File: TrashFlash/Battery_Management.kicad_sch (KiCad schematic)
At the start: 20 parts, among them IC701 BQ27426YZFR, IC702 BQ24230RGTR, IC703 BQ29732DSER, J701 USB4800-03-A, Q701 PMDPB30XNAX

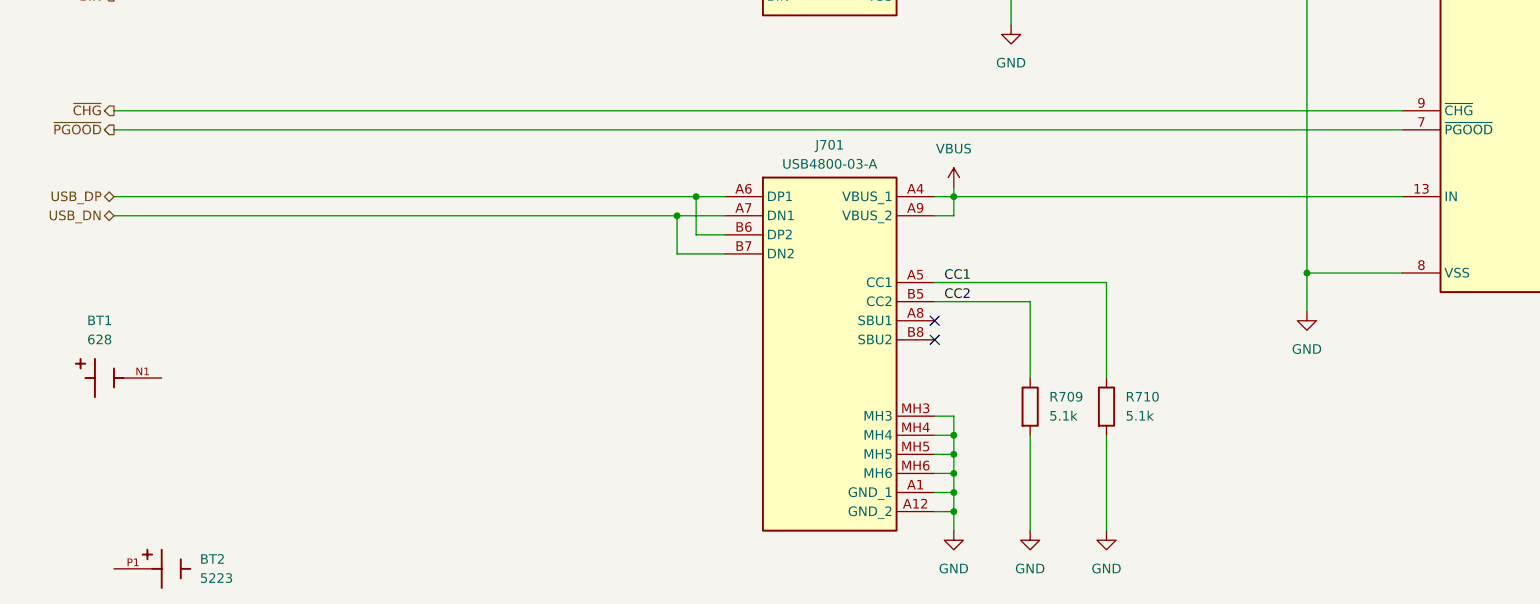
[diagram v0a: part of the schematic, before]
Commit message: Moved USB and added JTAG connector
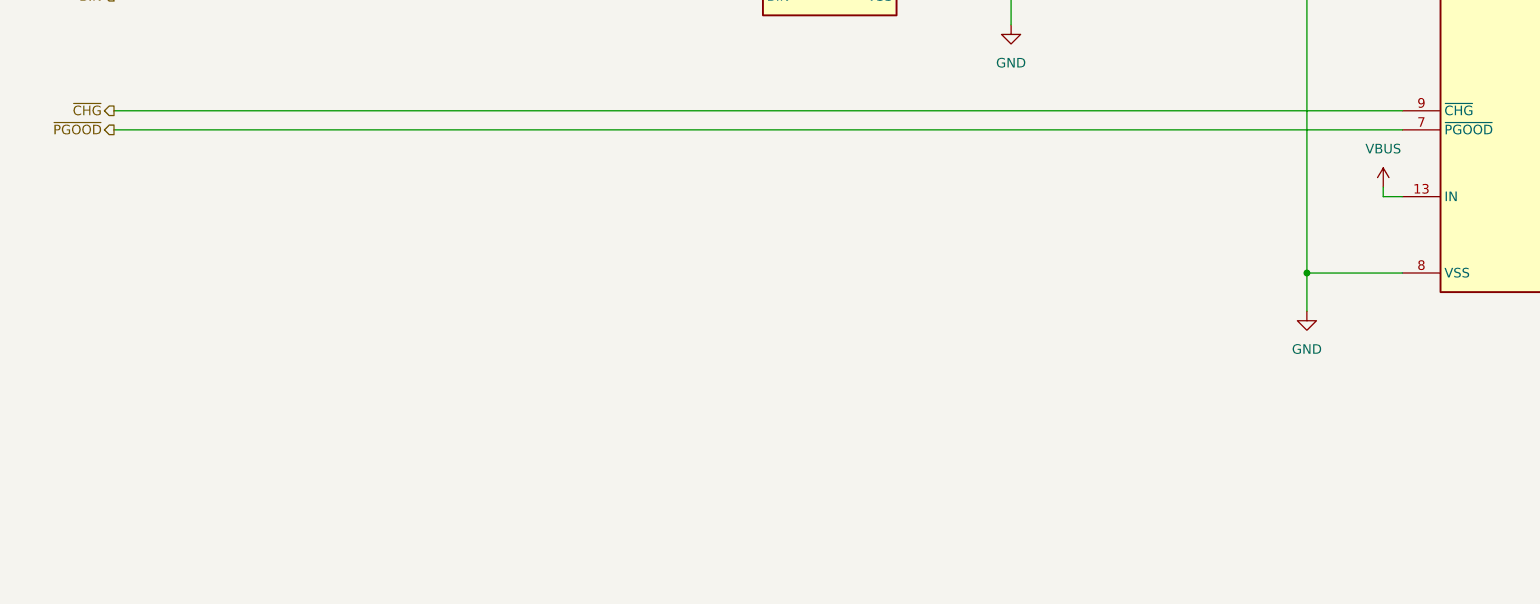
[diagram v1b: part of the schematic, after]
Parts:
- removed BT1: 628, TrashFlash:BAT_628, symbol TrashFlash:628
- removed BT2: 5223, TrashFlash:BAT_5223, symbol TrashFlash:5223
- removed J701: USB4800-03-A, USB480003A, symbol TrashFlash:USB4800-03-A
- removed R709, R710: 5.1k, Resistor_SMD:R_0402_1005Metric, symbol Device:R
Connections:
- no-connect marks 2 -> 0

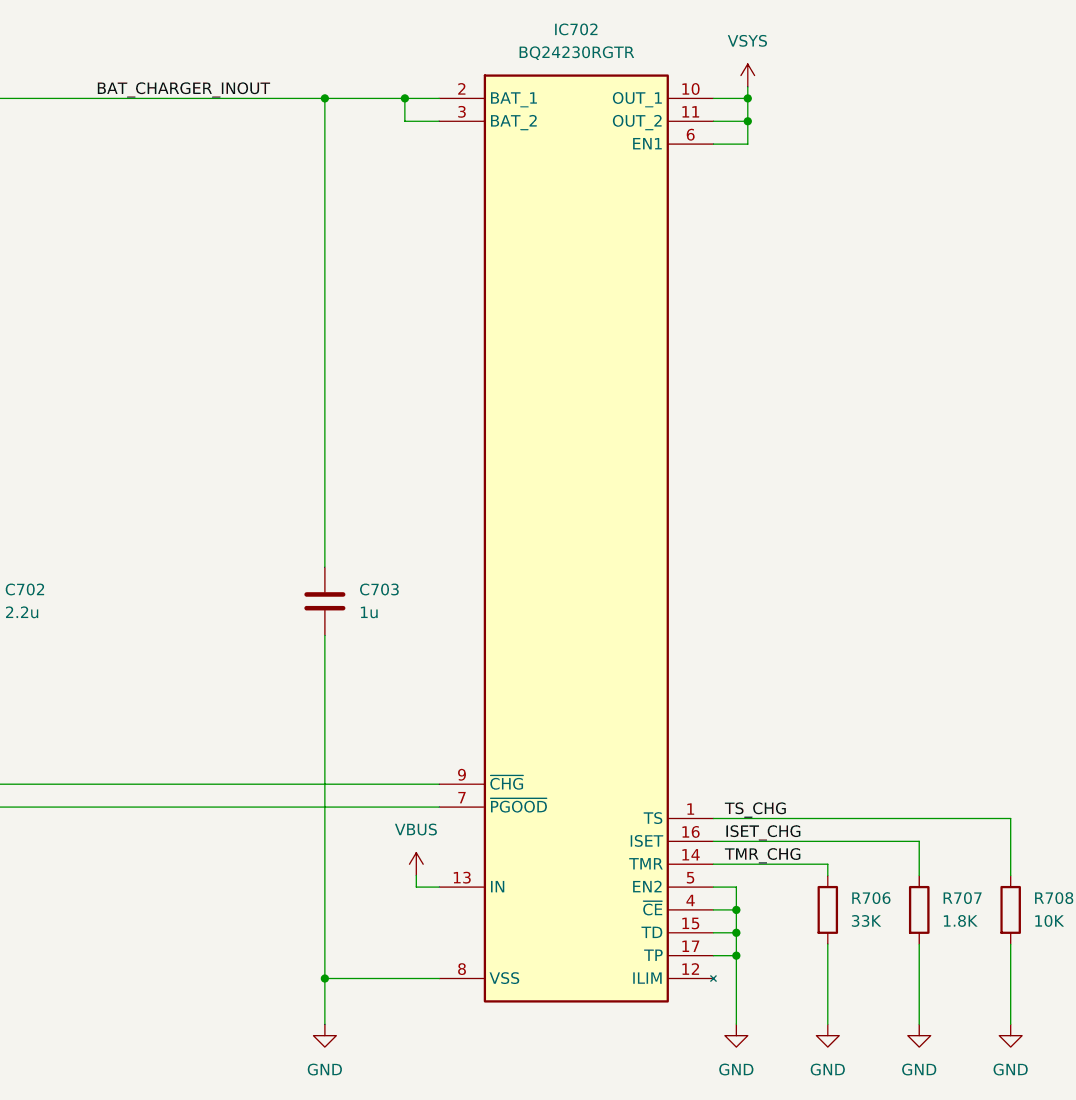
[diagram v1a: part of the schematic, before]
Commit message: Added Caps to Battery Charger
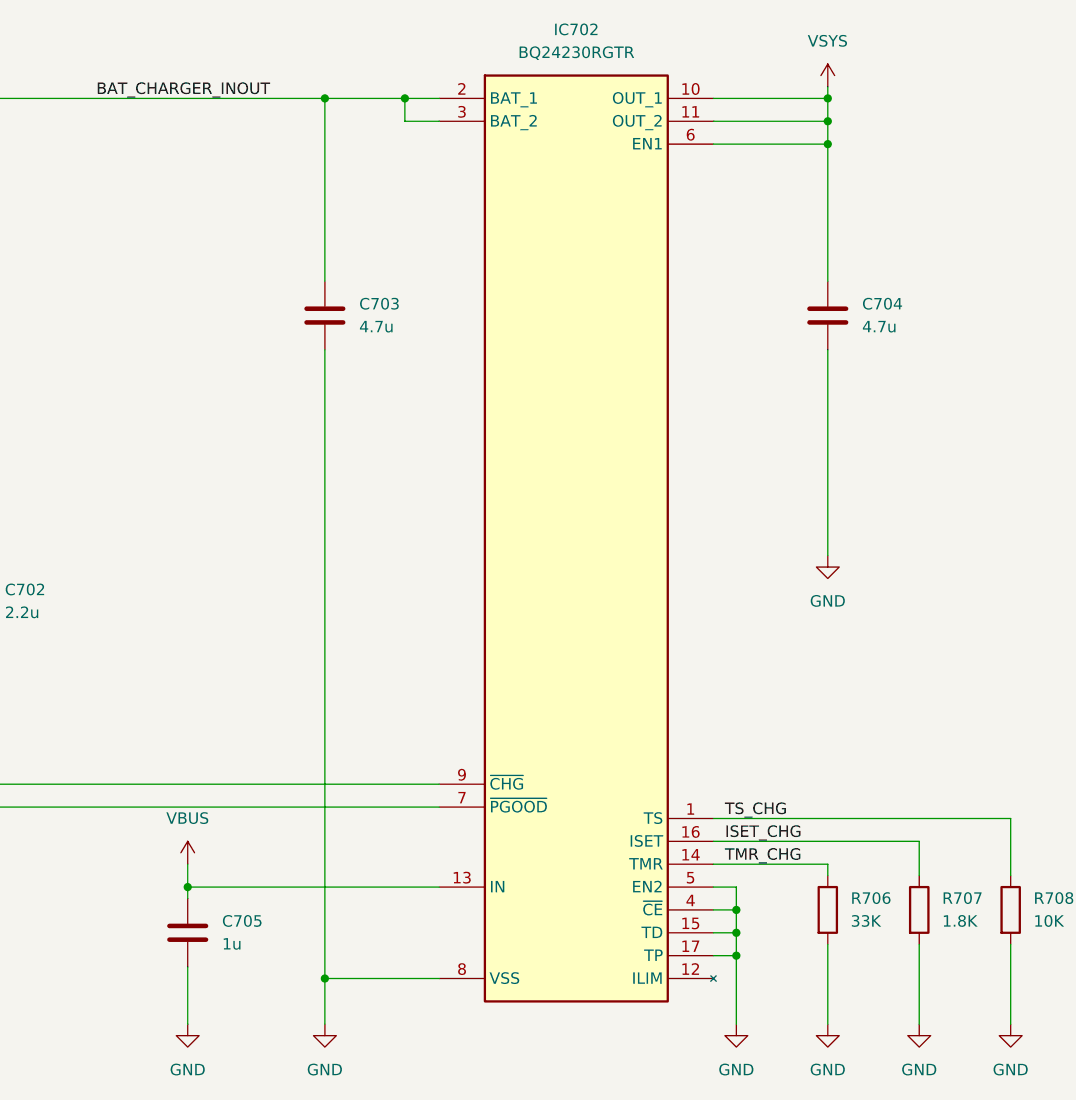
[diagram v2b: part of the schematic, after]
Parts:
- added C704: 4.7u, Capacitor_SMD:C_0603_1608Metric, symbol Device:C
- added C705: 1u, Capacitor_SMD:C_0603_1608Metric, symbol Device:C
- C703: value 1u -> 4.7u
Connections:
- net GND: now also C704.2, C705.2
- net VBUS: now also C705.1
- net VSYS: now also C704.1
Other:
- moved on the sheet: C703

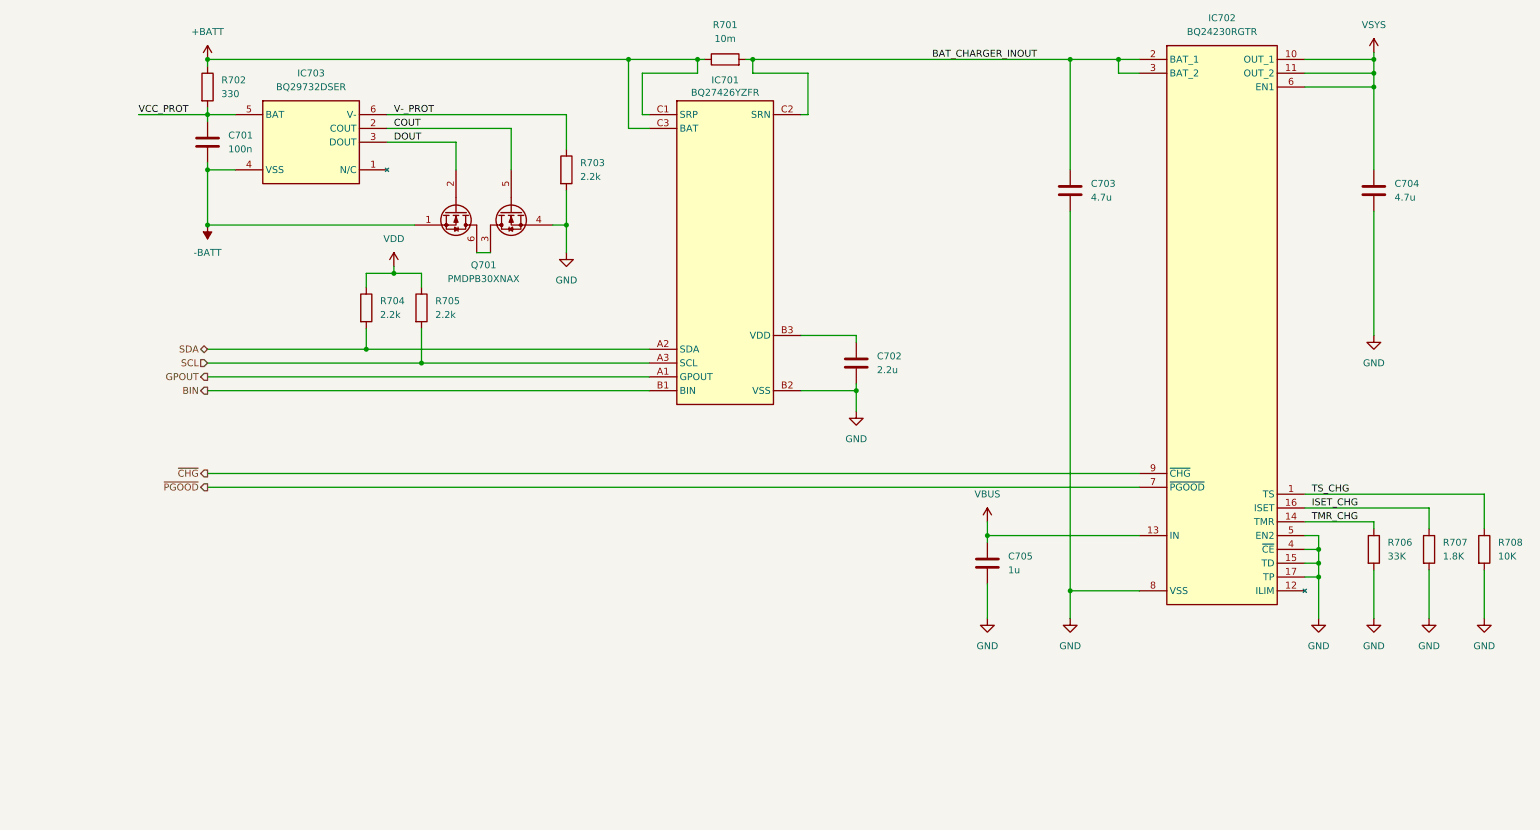
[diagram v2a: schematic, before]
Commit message: Added battery and connectors, Schematic remark for BQ297xx
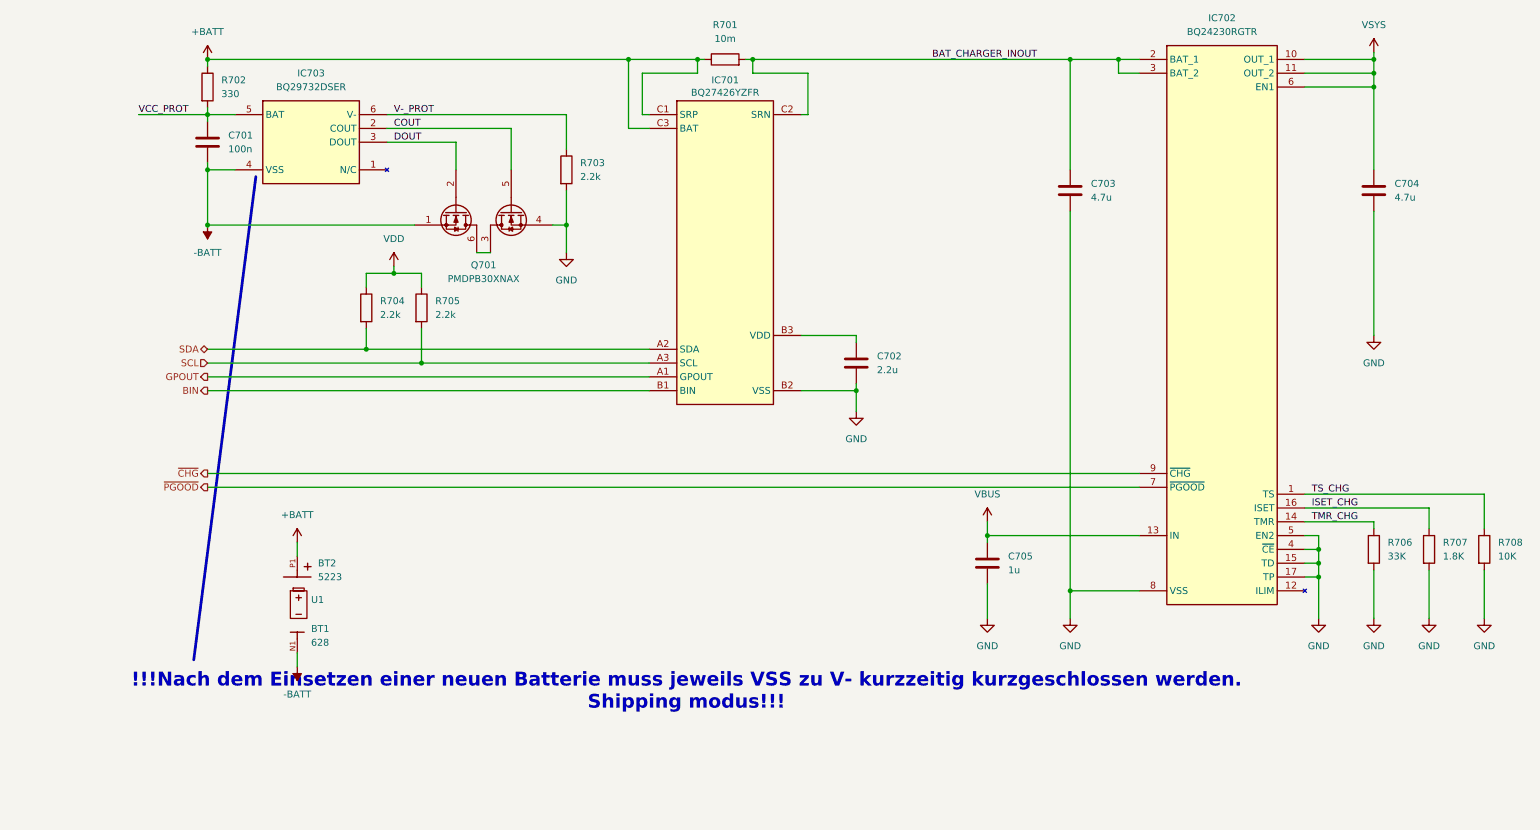
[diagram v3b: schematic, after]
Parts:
- added BT1: 628, TrashFlash:BAT_628, symbol TrashFlash:628
- added BT2: 5223, TrashFlash:BAT_5223, symbol TrashFlash:5223
- added U1: ~, TrashFlash:CR123A, symbol TrashFlash:CR123A
- IC701: footprint BGA9C50P3X3_158X162X62 -> TrashFlash:BGA9C50P3X3_158X162X62
- IC702: footprint QFN50P300X300X100-17N-D -> TrashFlash:QFN50P300X300X100-17N-D
- IC703: footprint SON50P150X150X80-6N -> TrashFlash:SON50P150X150X80-6N
- Q701: footprint PMDPB30XNAX -> TrashFlash:PMDPB30XNAX
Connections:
- net +BATT: now also BT2.P1
- net -BATT: now also BT1.N1, BT1.N2, BT1.N3
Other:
- note added: "!!!Nach dem Einsetzen einer neuen Batterie muss jeweils VSS zu V- kurzzeitig kurzgeschlossen werden. Shipping modus!!!"
